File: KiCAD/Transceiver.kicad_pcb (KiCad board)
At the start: 2 copper layers, 34 parts, among them J1 Conn_01x20_Female, J10 Conn_01x04_Female, J11 Conn_01x03_Female, J12 Conn_Coaxial, J13 Conn_Coaxial, J2 Conn_01x07_Female, J3 Conn_01x07_Female, J4 Conn_01x06_Female, J5 Conn_01x04_Female, J6 Conn_01x06_Female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

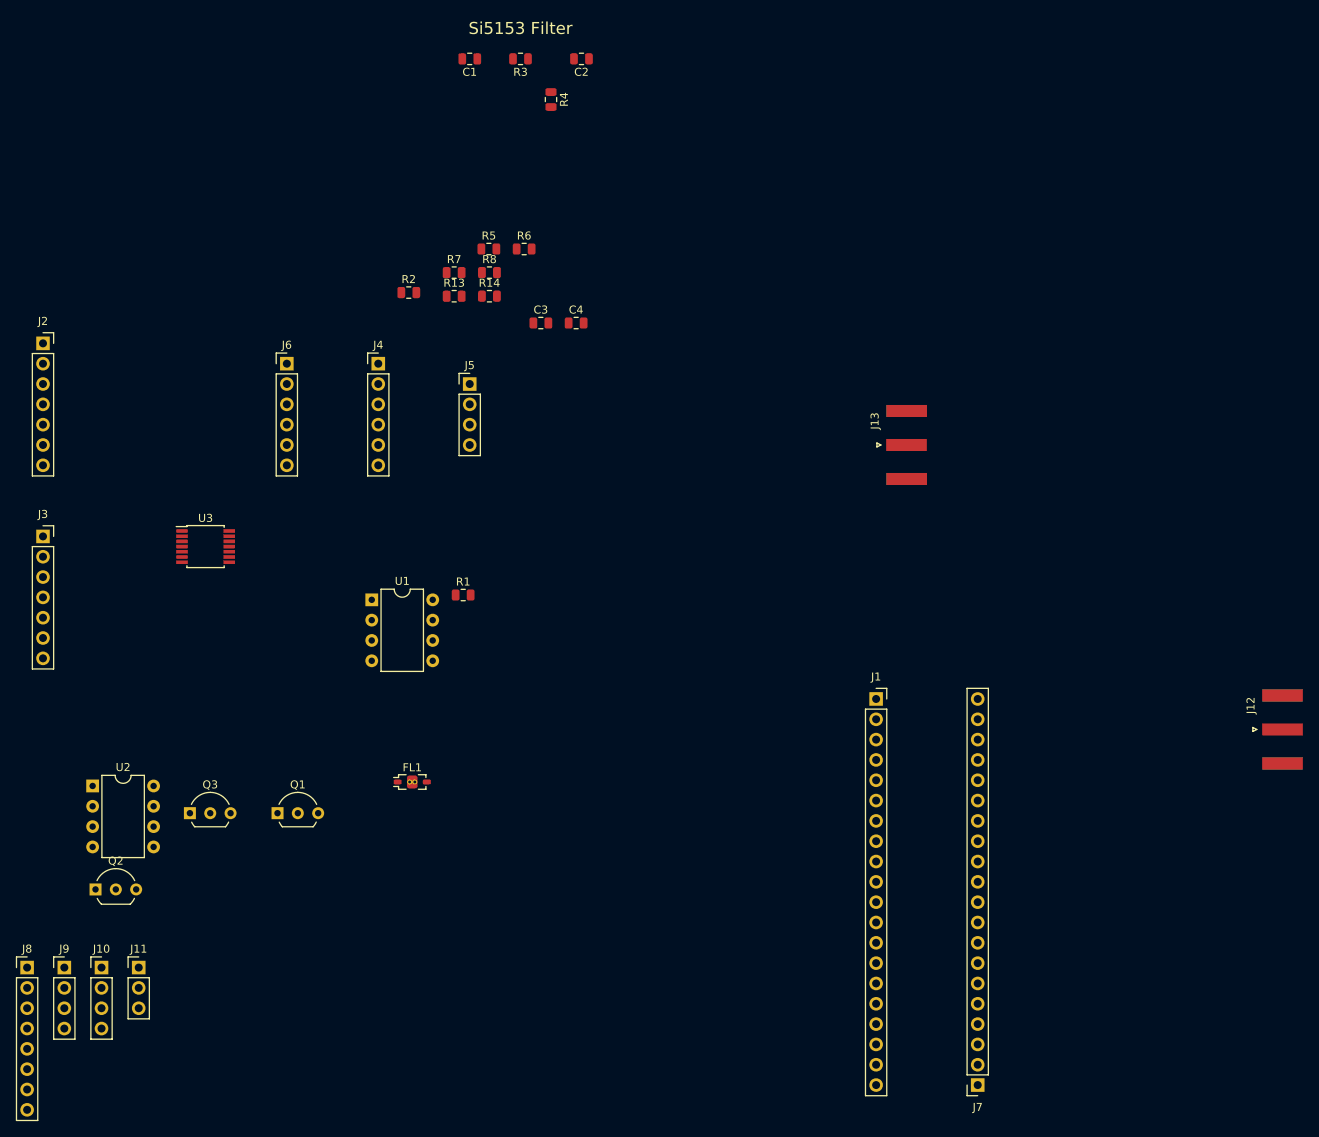
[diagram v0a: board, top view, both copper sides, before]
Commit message: Make PCB and change NPN and PNP for AM output
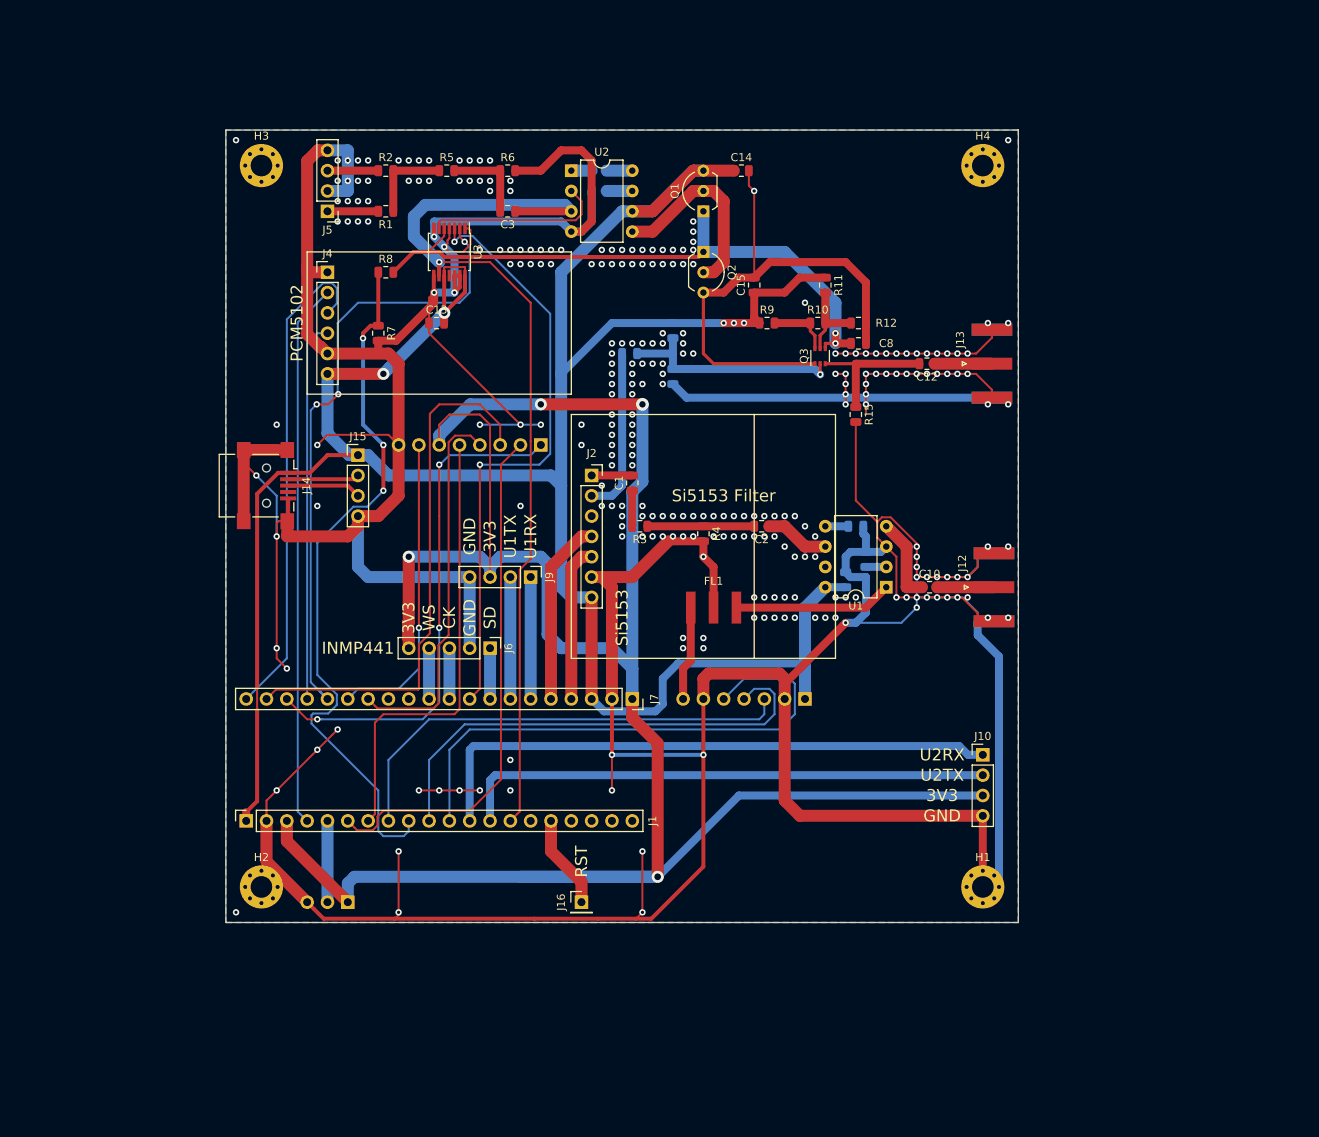
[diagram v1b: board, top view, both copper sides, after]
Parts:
- added C10: C, Capacitor_SMD:C_0805_2012Metric, F.Cu at (136.2, 113.0)
- added C11: C, Capacitor_SMD:C_0805_2012Metric, B.Cu at (127.0, 105.4)
- added C12: C, Capacitor_SMD:C_0805_2012Metric, F.Cu at (135.9, 85.1)
- added C13: C, Capacitor_SMD:C_0805_2012Metric, F.Cu at (74.6, 80.0)
- added C14: C, Capacitor_SMD:C_0805_2012Metric, F.Cu at (112.7, 61.0)
- added C15: C, Capacitor_SMD:C_0805_2012Metric, F.Cu at (114.3, 75.3)
- added C5: C, Capacitor_SMD:C_0805_2012Metric, B.Cu at (128.3, 109.6)
- added C6: C, Capacitor_SMD:C_0805_2012Metric, B.Cu at (94.9, 63.5)
- added C7: C, Capacitor_SMD:C_0805_2012Metric, B.Cu at (94.9, 61.0)
- added C8: C, Capacitor_SMD:C_0805_2012Metric, F.Cu at (127.3, 82.5)
- added C9: 100n, Capacitor_SMD:C_0805_2012Metric, B.Cu at (125.7, 112.1)
- added H1: MountingHole_Pad, MountingHole:MountingHole_2.7mm_M2.5_Pad_Via, F.Cu at (142.9, 150.5)
- added H2: MountingHole_Pad, MountingHole:MountingHole_2.7mm_M2.5_Pad_Via, F.Cu at (52.7, 150.5)
- added H3: MountingHole_Pad, MountingHole:MountingHole_2.7mm_M2.5_Pad_Via, F.Cu at (52.7, 60.3)
- added H4: MountingHole_Pad, MountingHole:MountingHole_2.7mm_M2.5_Pad_Via, F.Cu at (142.9, 60.3)
- added J14: USB_B_Mini, Connector_USB:USB_Mini-B_Lumberg_2486_01_Horizontal, F.Cu at (53.3, 100.3)
- added J15: Conn_01x04_Female, Connector_PinHeader_2.54mm:PinHeader_1x04_P2.54mm_Vertical, F.Cu at (64.8, 96.5)
- added J16: Conn_01x01_Female, Connector_PinHeader_2.54mm:PinHeader_1x01_P2.54mm_Vertical, F.Cu at (92.7, 152.4)
- added R10: R, Resistor_SMD:R_0805_2012Metric, F.Cu at (122.3, 80.0)
- added R11: R, Resistor_SMD:R_0805_2012Metric, F.Cu at (123.2, 75.3)
- added R12: R, Resistor_SMD:R_0805_2012Metric, F.Cu at (127.3, 80.0)
- added R15: R, Resistor_SMD:R_0805_2012Metric, F.Cu at (127.0, 91.4)
- added R9: R, Resistor_SMD:R_0805_2012Metric, F.Cu at (115.9, 80.0)
- C4, J11, J3, J8, R13, R14: moved to B.Cu
- FL1: footprint Filter:Filter_Mini-Circuits_FV1206-7 -> Ceramic_Filter:SFECK
- J6: value Conn_01x06_Female -> Conn_01x05_Female; footprint Connector_PinHeader_2.54mm:PinHeader_1x06_P2.54mm_Vertical -> Connector_PinHeader_2.54mm:PinHeader_1x05_P2.54mm_Vertical
- Q3: value 2N2219 -> MMDT3946; footprint Package_TO_SOT_THT:TO-92L_Inline_Wide -> Package_TO_SOT_SMD:SOT-363_SC-70-6
- U2: value AD8001AN -> LM386
- moved J10 113.3 mm to (142.9, 134.0)
- moved Q2 110.1 mm to (108.0, 71.1), turned to 270 degrees
- moved U2 97.4 mm to (91.4, 61.0)
- moved J3 97.4 mm to (120.7, 127.0), turned to 90 degrees
- moved Q3 97.3 mm to (122.5, 84.1), turned to 90 degrees
- moved Q1 92.2 mm to (108.0, 66.0), turned to 90 degrees
- moved J8 91.6 mm to (87.6, 95.2), turned to 90 degrees
- moved J1 80.2 mm to (50.8, 142.2), turned to 90 degrees
- moved J9 76.0 mm to (86.4, 111.8), turned to 270 degrees
- moved J2 70.5 mm to (94.0, 99.1)
- moved J7 64.8 mm to (99.1, 127.0), turned to 270 degrees
- moved U1 64.3 mm to (130.8, 113.0), turned to 180 degrees
- moved C2 62.6 mm to (115.2, 105.4)
- moved R3 60.3 mm to (100.0, 105.4)
- moved R4 57.5 mm to (108.0, 106.3)
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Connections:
- FL1 pad 1: /AD9833 Filter/MClk_Fi -> /MClk_Fi
- FL1 pad 3: /AD9833 Filter/IN_A_Out -> /IN_A_Out
- J10 pad 1: +5V -> /USART2_RX
- J10 pad 2: /USART2_RX -> /USART2_TX
- J10 pad 3: /USART2_TX -> +3V3
- J12 pad 1: Net-(J12-Pad1) -> /FM_Out
- J3 pad 6: Net-(J3-Pad6) -> GND
- J6 pad 1: GND -> /I2Sb_SD
- J6 pad 2: +3V3 -> GND
- J6 pad 3: /I2Sb_SD -> /I2Sb_CK
- J6 pad 4: GND -> /I2Sb_WS
- J6 pad 5: /I2Sb_WS -> +3V3
- J9 pad 1: +5V -> /USART1_RX
- J9 pad 2: /USART1_RX -> /USART1_TX
- J9 pad 3: /USART1_TX -> +3V3
- Q3 pad 1: /AM_Out -> GND
- Q3 pad 3: /AM Module/H1 -> Net-(C12-Pad2)
- R13 pad 1: /AM Module/H1 -> +5V
- U1 pad 2: /IN_B_Out -> Net-(C5-Pad1)
- U2 pad 5: Net-(U2-Pad5) -> Net-(Q1-Pad2)
- U2 pad 6: Net-(Q1-Pad2) -> +5V
- U2 pad 7: +5V -> Net-(C6-Pad2)
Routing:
- net GND: track 0.00 -> 866.0 mm, vias 0 -> 271
- net +5V: track 0.00 -> 316.9 mm, vias 0 -> 5
- net +3V3: track 0.00 -> 291.4 mm, vias 0 -> 4
- net /FBBFin: track 0.00 -> 115.7 mm, vias 0 -> 1
- net /FBBFout: track 0.00 -> 89.2 mm, vias 0 -> 3
- net /SCL_1: track 0.00 -> 78.6 mm, vias 0 -> 3
- net /AM Module/H1: track 0.00 -> 78.5 mm, vias 0 -> 2
- net /SDA_1: track 0.00 -> 74.7 mm, vias 0 -> 2
- net /USART2_RX: track 0.00 -> 73.7 mm
- net /I2Sa_CK: track 0.00 -> 68.1 mm
- net /SS_AD9833: track 0.00 -> 67.9 mm
- net /Nokia_DC: track 0.00 -> 67.9 mm
- net /USART2_TX: track 0.00 -> 66.9 mm
- net /SPI5_NSS: track 0.00 -> 65.7 mm
- net /Nokia_RST: track 0.00 -> 64.6 mm, vias 0 -> 3
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- added copper zone on B.Cu, net GND
- added copper zone on F.Cu, net GND
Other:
- board outline added: 99.1 x 99.1 mm
- net class 0.5mm added: clearance 0.2, trace_width 0.5, via_dia 0.8, via_drill 0.4
- board text added: "3V3"
- board text added: "5110"
- board text added: "5V"
- board text added: "AD9833"
- board text added: "CK"
- board text added: "CS"
- board text added: "D+"
- board text added: "D-"
- board text added: "DC"
- board text added: "GND"
- board text added: "INMP441"
- board text added: "IR"
- board text added: "Light"
- board text added: "MOSI"
- board text added: "OUT"
- board text added: "PCM5102"
- board text added: "RST"
- board text added: "SCK"
- board text added: "SD"
- board text added: "Si5153"
- board text added: "U1RX"
- board text added: "U1TX"
- board text added: "U2RX"
- board text added: "U2TX"
- board text added: "WS"

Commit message: Schematics and PCB update
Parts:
- removed FL1: EMI_Filter_LCL, Ceramic_Filter:SFECK
- added BT1: Battery_Cell, Battery:BatteryHolder_Keystone_103_1x20mm, F.Cu at (112.9, 142.2)
- added C16: 100n, Capacitor_SMD:C_0805_2012Metric, F.Cu at (130.8, 114.6)
- added C17: 100n, Capacitor_SMD:C_0805_2012Metric, F.Cu at (129.5, 121.0)
- added D1: LED, LED_SMD:LED_0603_1608Metric_Castellated, F.Cu at (85.9, 148.6)
- added D2: LED, LED_SMD:LED_0603_1608Metric_Castellated, F.Cu at (100.8, 152.4)
- added J17: Barrel_Jack_Switch, Connector_BarrelJack:BarrelJack_Horizontal, F.Cu at (135.9, 69.5)
- added J18: Conn_01x04_Female, Connector_PinHeader_2.54mm:PinHeader_1x04_P2.54mm_Vertical, F.Cu at (144.1, 118.7)
- added J19: Conn_01x01_Female, Connector_PinHeader_2.54mm:PinHeader_1x01_P2.54mm_Vertical, F.Cu at (144.1, 69.2)
- added J20: Conn_01x01_Female, Connector_PinHeader_2.54mm:PinHeader_1x01_P2.54mm_Vertical, F.Cu at (139.1, 151.8)
- added J21: Conn_01x01_Female, Connector_PinHeader_2.54mm:PinHeader_1x01_P2.54mm_Vertical, F.Cu at (54.0, 67.3)
- added J22: Conn_01x01_Female, Connector_PinHeader_2.54mm:PinHeader_1x01_P2.54mm_Vertical, F.Cu at (75.6, 153.0)
- added J23: Conn_01x01_Female, Connector_PinHeader_2.54mm:PinHeader_1x01_P2.54mm_Vertical, F.Cu at (106.0, 58.4)
- added J24: Conn_01x01_Female, Connector_PinHeader_2.54mm:PinHeader_1x01_P2.54mm_Vertical, F.Cu at (115.6, 67.9)
- added Q4: 2N2219, Package_TO_SOT_THT:TO-92L_Inline_Wide, F.Cu at (63.5, 116.8)
- added R16: R, Resistor_SMD:R_0805_2012Metric, F.Cu at (80.3, 148.6)
- added R17: R, Resistor_SMD:R_0805_2012Metric, F.Cu at (106.3, 152.4)
- added R18: R, Resistor_SMD:R_0805_2012Metric, B.Cu at (66.0, 121.6)
- added R19: R, Resistor_SMD:R_0805_2012Metric, F.Cu at (125.7, 121.0)
- added U4: AMS1117-5.0, Package_TO_SOT_SMD:SOT-223-3_TabPin2, F.Cu at (123.2, 63.5)
- C11, C4, C5, C9, R13, R14: moved to F.Cu
- J10: value Conn_01x04_Female -> Conn_01x05_Female; footprint Connector_PinHeader_2.54mm:PinHeader_1x04_P2.54mm_Vertical -> Connector_PinHeader_2.54mm:PinHeader_1x05_P2.54mm_Vertical
- U1: footprint Package_DIP:DIP-8_W7.62mm -> Package_SO:SOIC-8-1EP_3.9x4.9mm_P1.27mm_EP2.29x3mm
- moved C4 22.0 mm to (120.3, 87.6)
- moved R3 20.0 mm to (120.0, 105.1), turned to 90 degrees
- moved R14 19.8 mm to (123.8, 88.6)
- moved J2 19.0 mm to (113.0, 99.1)
- moved C1 18.6 mm to (117.2, 104.1), turned to 180 degrees
- moved R13 15.7 mm to (119.7, 83.2), turned to 0 degrees
- moved J3 10.2 mm to (110.5, 125.7), turned to 270 degrees
- moved R4 9.36 mm to (117.2, 108.0), turned to 180 degrees
- moved C10 7.73 mm to (137.5, 105.4)
- moved J12 7.71 mm to (145.4, 105.4)
- moved C2 6.28 mm to (121.0, 108.0)
- moved U1 6.23 mm to (128.3, 107.3)
- moved C5 6.02 mm to (134.0, 107.6)
- moved C11 3.73 mm to (125.7, 101.9), turned to 90 degrees
- moved J10 2.84 mm to (144.1, 131.4)
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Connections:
- J1 pad 15: Net-(J1-Pad15) -> /LED2
- J1 pad 19: /LED -> /LED1
- J1 pad 20: Net-(J1-Pad20) -> /Vbat
- J10 pad 1: /USART2_RX -> +5V
- J10 pad 2: /USART2_TX -> /USART2_RX
- J10 pad 3: +3V3 -> /USART2_TX
- J10 pad 4: GND -> +3V3
- J2 pad 1: /Clk0_Fi -> /Clk1_Fi
- J2 pad 2: /Clk1_Fi -> Net-(J2-Pad2)
- J2 pad 3: Net-(J2-Pad3) -> /Clk0_Fi
- J7 pad 15: /Nokia_Light -> /Nokia_Light_CMD
- U3 pad 2: /SCL_1 -> /SCL_0
- U3 pad 3: /SDA_1 -> /SDA_0
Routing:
- net GND: track 866.0 -> 640.3 mm, vias 271 -> 227
- net +5V: track 316.9 -> 459.9 mm, vias 5 -> 12
- net /SCL_0: track 23.2 -> 99.5 mm, vias 0 -> 2
- net /SDA_0: track 19.6 -> 95.8 mm, vias 0 -> 4
- net +3V3: track 291.4 -> 268.6 mm, vias 4 -> 10
- net Net-(C4-Pad1): track 28.4 -> 9.42 mm, vias 1 -> 0
- net /Vbat: track 0.00 -> 17.3 mm
- net /IN_A_Out: track 19.8 -> 4.45 mm
- net /SCL_1: track 78.6 -> 93.7 mm
- net /Nokia_Light: track 38.4 -> 23.7 mm, vias 1 -> 0
- net Net-(J17-Pad1): track 0.00 -> 13.3 mm
- net /SS_AD9833: track 67.9 -> 55.2 mm
- net /LED1: track 0.00 -> 11.6 mm
- net Net-(C2-Pad2): track 13.4 -> 4.25 mm
- net Net-(C16-Pad1): track 0.00 -> 8.84 mm
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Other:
- board text added: "3"
- board text added: "AM OUTPUT"
- board text added: "Battery CR2025 CR2032"
- board text added: "F4IFB_TX001"
- board text added: "FM OUTPUT"
- board text added: "G"
- board text added: "JLCJLCJLCJLC"
- board text added: "L"
- board text added: "MiniF4 / WeAct Studio RECOMMAND STM32F411xC/D BE AWARE BACK ON TOP"
- board text added: "R"
- board text added: "SCL1"
- board text added: "SDA1"
- board text added: "U = 6-9V MAX:12V I max (Sumulation) 400mA See git repo for update informations."
- board text added: "https://github.com/schiad/AM_FM_Transceiver.git"
